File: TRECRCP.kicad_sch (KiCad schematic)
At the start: 46 parts, among them K1 12v Coil Relay, K2 12v Coil Relay, K5 Fujitsu_FTR-LYCA005x, K6 Fujitsu_FTR-LYCA005x, K7 Fujitsu_FTR-LYCA005x, Q2 STF40NF03L, Q3 STF40NF03L, Q4 STF40NF03L, SW1 Dispatch2, SW1 Maint/Off/On Switch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

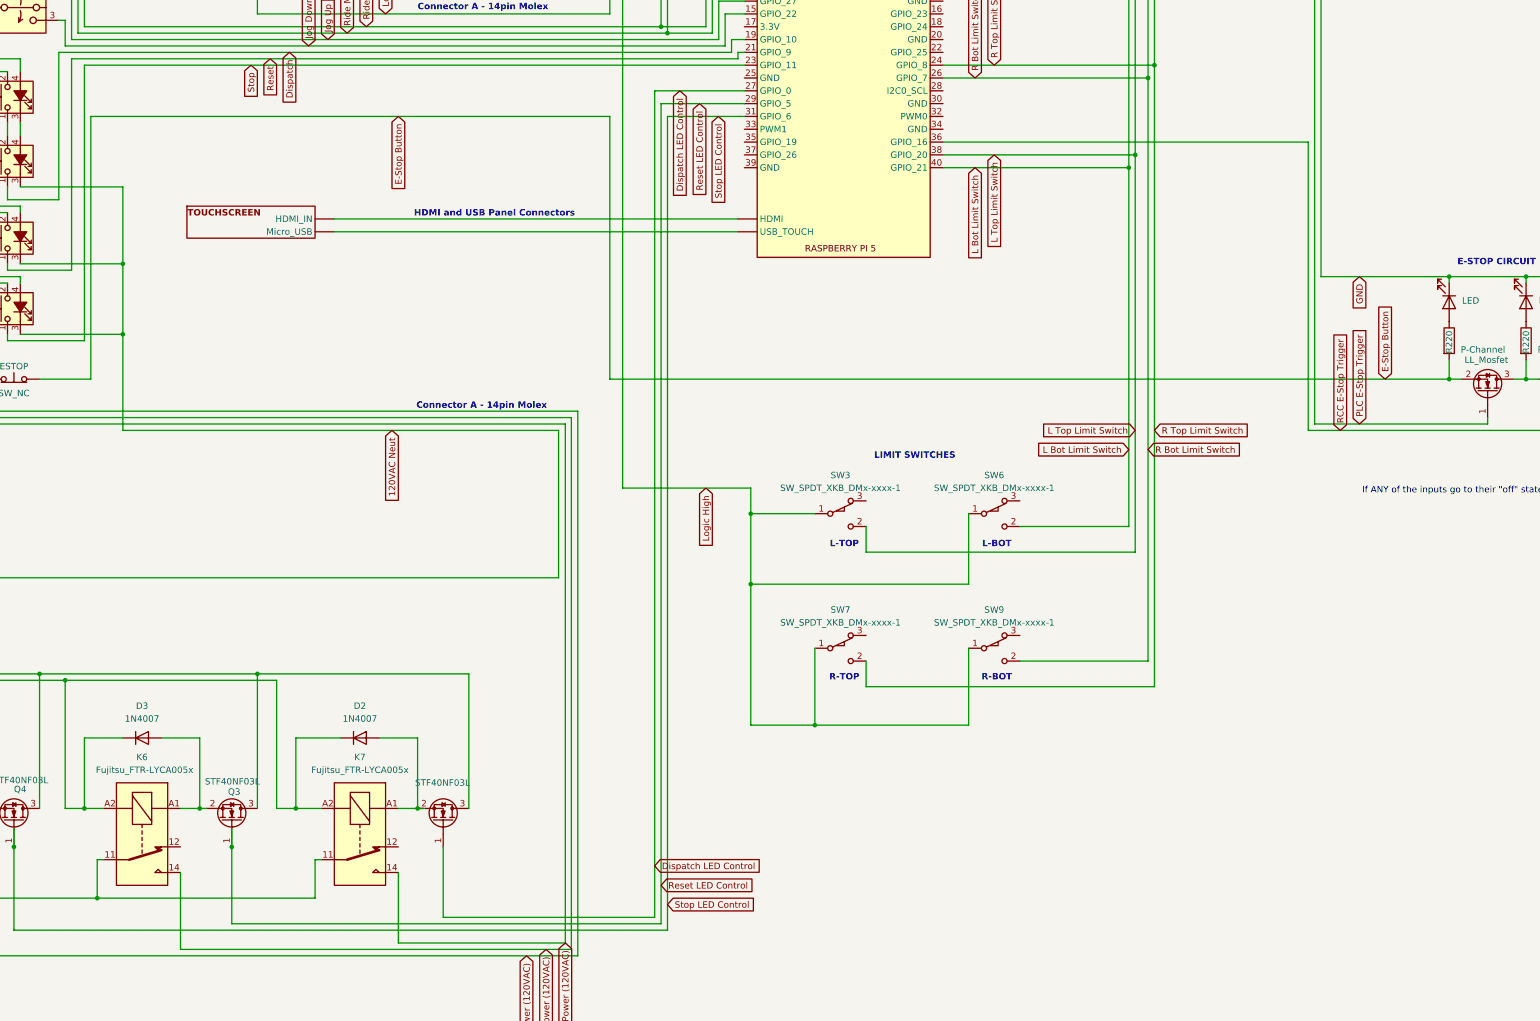
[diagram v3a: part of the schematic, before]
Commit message: update w/ new RCC pin #s
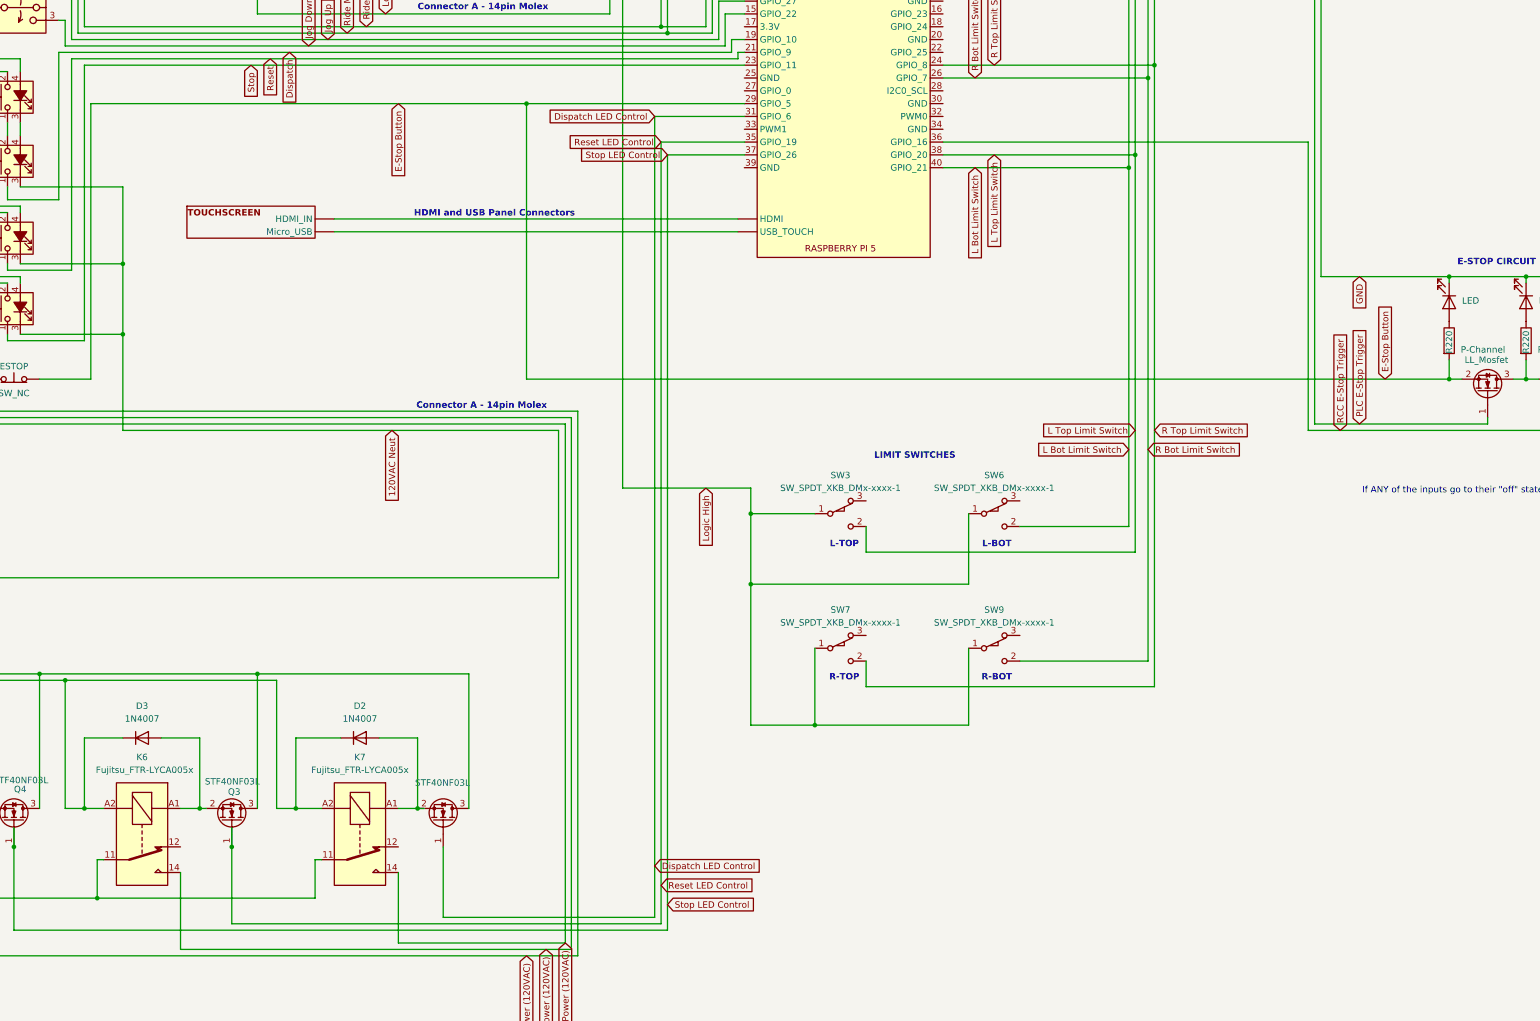
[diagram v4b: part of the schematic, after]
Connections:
- net Dispatch LED Control: now also RCC1.31 (GPIO_6); no longer RCC1.27 (GPIO_0)
- net E-Stop Button: now also RCC1.29 (GPIO_5)
- net Reset LED Control: now also RCC1.35 (GPIO_19); no longer RCC1.29 (GPIO_5)
- net Stop LED Control: now also RCC1.37 (GPIO_26); no longer RCC1.31 (GPIO_6)
- net at RCC1. (USB-C): now also U2.3 (USB-C); no longer U3. (Micro_USB)
- new net: RCC1. (USB-C), U3. (Micro_USB)
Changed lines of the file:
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@@
 	)
 	(junction
+		(at 227.33 168.91)
+		(diameter 0)
+		(color 0 0 0 0)
+	)
+	(junction
 		(at 271.78 250.19)
 		(diameter 0)
@@
 	(wire
 		(pts
-			(xy 252.73 166.37) (xy 252.73 330.2)
+			(xy 252.73 171.45) (xy 252.73 330.2)
 		)
 		(stroke
@@
 	(wire
 		(pts
-			(xy 252.73 166.37) (xy 270.51 166.37)
-		)
-		(stroke
-			(width 0)
-			(type default)
-		)
-	)
-	(wire
-		(pts
 			(xy 204.47 96.52) (xy 298.45 96.52)
 		)
@@
 	(wire
 		(pts
-			(xy 140.97 223.52) (xy 140.97 171.45)
+			(xy 140.97 223.52) (xy 140.97 168.91)
 		)
 		(stroke
@@
 	(wire
 		(pts
+			(xy 255.27 179.07) (xy 270.51 179.07)
+		)
+		(stroke
+			(width 0)
+			(type default)
+		)
+	)
+	(wire
+		(pts
 			(xy 210.82 316.23) (xy 210.82 330.2)
 		)
@@
 	(wire
 		(pts
-			(xy 254 168.91) (xy 254 331.47)
+			(xy 254 176.53) (xy 254 331.47)
 		)
 		(stroke
@@
 	(wire
 		(pts
+			(xy 254 176.53) (xy 270.51 176.53)
+		)
+		(stroke
+			(width 0)
+			(type default)
+		)
+	)
+	(wire
+		(pts
 			(xy 347.98 64.77) (xy 347.98 179.07)
 		)
@@
 	(wire
 		(pts
-			(xy 254 168.91) (xy 270.51 168.91)
-		)
-		(stroke
-			(width 0)
-			(type default)
-		)
-	)
-	(wire
-		(pts
 			(xy 114.3 321.31) (xy 114.3 337.82)
 		)
@@
 	(wire
 		(pts
-			(xy 255.27 171.45) (xy 270.51 171.45)
-		)
-		(stroke
-			(width 0)
-			(type default)
-		)
-	)
-	(wire
-		(pts
 			(xy 127 160.02) (xy 127 162.56)
 		)
@@
 	(wire
 		(pts
+			(xy 227.33 168.91) (xy 270.51 168.91)
+		)
+		(stroke
+			(width 0)
+			(type default)
+			(color 255 0 0 1)
+		)
+	)
+	(wire
+		(pts
 			(xy 185.42 326.39) (xy 142.24 326.39)
 		)
@@
 	(wire
 		(pts
-			(xy 255.27 171.45) (xy 255.27 332.74)
+			(xy 255.27 179.07) (xy 255.27 332.74)
 		)
 		(stroke
@@
 	(wire
 		(pts
+			(xy 252.73 171.45) (xy 270.51 171.45)
+		)
+		(stroke
+			(width 0)
+			(type default)
+		)
+	)
+	(wire
+		(pts
 			(xy 383.54 76.2) (xy 383.54 232.41)
 		)
@@
 	(wire
 		(pts
-			(xy 243.84 171.45) (xy 243.84 223.52)
-		)
-		(stroke
-			(width 0)
-			(type default)
-			(color 255 0 0 1)
-		)
-	)
-	(wire
-		(pts
 			(xy 101.6 160.02) (xy 127 160.02)
 		)
@@
 	(wire
 		(pts
-			(xy 140.97 171.45) (xy 243.84 171.45)
+			(xy 140.97 168.91) (xy 227.33 168.91)
 		)
 		(stroke
@@
 	(wire
 		(pts
-			(xy 243.84 223.52) (xy 410.21 223.52)
+			(xy 227.33 223.52) (xy 410.21 223.52)
 		)
 		(stroke
@@
 	(wire
 		(pts
+			(xy 227.33 168.91) (xy 227.33 223.52)
+		)
+		(stroke
+			(width 0)
+			(type default)
+			(color 255 0 0 1)
+		)
+	)
+	(wire
+		(pts
 			(xy 254 67.31) (xy 254 153.67)
 		)
@@
 	(global_label "Dispatch LED Control"
 		(shape input)
-		(at 257.7235 166.37 270)
+		(at 252.73 171.45 180)
 		(fields_autoplaced yes)
 		(effects
@@
 		)
 		(property "Intersheetrefs" "${INTERSHEET_REFS}"
-			(at 257.7235 189.7958 90)
+			(at 229.3042 171.45 0)
 			(effects
 				(font
@@
 	(global_label "Reset LED Control"
 		(shape input)
-		(at 261.62 168.91 270)
+		(at 254 176.53 180)
 		(fields_autoplaced yes)
 		(effects
@@
 		)
 		(property "Intersheetrefs" "${INTERSHEET_REFS}"
-			(at 261.62 189.3726 90)
+			(at 233.5374 176.53 0)
 			(effects
 				(font
@@
 	(global_label "E-Stop Button"
 		(shape input)
-		(at 201.93 171.45 270)
+		(at 201.93 168.91 270)
 		(fields_autoplaced yes)
 		(effects
@@
 		)
 		(property "Intersheetrefs" "${INTERSHEET_REFS}"
-			(at 201.93 188.5258 90)
+			(at 201.93 185.9858 90)
 			(effects
 				(font
@@
 	(global_label "Stop LED Control"
 		(shape input)
-		(at 265.3624 171.45 270)
+		(at 255.27 179.07 180)
 		(fields_autoplaced yes)
 		(effects
@@
 		)
 		(property "Intersheetrefs" "${INTERSHEET_REFS}"
-			(at 265.3624 190.9448 90)
+			(at 235.7752 179.07 0)
 			(effects
 				(font

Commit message: update mosfets
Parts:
- LL_Mosfet: value STF40NF03L -> IRLZ44NPDB
- Q2, Q3, Q4: value STF40NF03L -> IRLZ44NPBF
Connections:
- net at RCC1. (USB-C): now also U2.3 (USB-C); no longer U3. (Micro_USB)
- new net: RCC1. (USB-C), U3. (Micro_USB)
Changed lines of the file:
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@@
 			)
 		)
-		(property "Value" "STF40NF03L"
-			(at 205.232 303.53 90)
+		(property "Value" "IRLZ44NPBF"
+			(at 206.248 305.308 90)
 			(effects
 				(font
@@
 				)
 				(justify left)
-			)
-		)
-		(property "Value" "STF40NF03L"
-			(at 163.576 303.276 90)
+				(hide yes)
+			)
+		)
+		(property "Value" "IRLZ44NPBF"
+			(at 163.576 305.562 90)
 			(effects
 				(font
@@
 			)
 		)
-		(property "Value" "STF40NF03L"
+		(property "Value" "IRLZ44NPDB"
 			(at 181.102 49.784 90)
 			(effects
@@
 				)
 				(justify left)
-			)
-		)
-		(property "Value" "STF40NF03L"
-			(at 121.666 303.022 90)
-			(effects
-				(font
+				(hide yes)
+			)
+		)
+		(property "Value" "IRLZ44NPBF"
+			(at 119.888 305.308 90)
+			(effects
+				(font

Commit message: change wiring of lim switches for plc
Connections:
- net L Bot Limit Switch: now also SW6.3 (C); no longer SW6.2 (B)
- net L Top Limit Switch: now also SW3.3 (C); no longer SW3.2 (B)
- net R Bot Limit Switch: now also SW9.3 (C); no longer SW9.2 (B)
- net R Top Limit Switch: now also SW7.3 (C); no longer SW7.2 (B)
- net at RCC1. (USB-C): now also U2.3 (USB-C); no longer U3. (Micro_USB)
- new net: RCC1. (USB-C), U3. (Micro_USB)
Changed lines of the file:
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@@
 	(wire
 		(pts
+			(xy 294.64 247.65) (xy 298.45 247.65)
+		)
+		(stroke
+			(width 0)
+			(type default)
+		)
+	)
+	(wire
+		(pts
 			(xy 254 67.31) (xy 341.63 67.31)
 		)
@@
 	(wire
 		(pts
-			(xy 294.64 252.73) (xy 294.64 257.81)
-		)
-		(stroke
-			(width 0)
-			(type default)
-		)
-	)
-	(wire
-		(pts
 			(xy 59.69 119.38) (xy 59.69 281.94)
 		)
@@
 	(wire
 		(pts
+			(xy 299.72 284.48) (xy 351.79 284.48)
+		)
+		(stroke
+			(width 0)
+			(type default)
+		)
+	)
+	(wire
+		(pts
 			(xy 186.69 67.31) (xy 186.69 64.77)
 		)
@@
 	(wire
 		(pts
+			(xy 325.12 247.65) (xy 328.93 247.65)
+		)
+		(stroke
+			(width 0)
+			(type default)
+		)
+	)
+	(wire
+		(pts
 			(xy 22.86 107.95) (xy 29.21 107.95)
 		)
@@
 	(wire
 		(pts
+			(xy 298.45 247.65) (xy 298.45 257.81)
+		)
+		(stroke
+			(width 0)
+			(type default)
+		)
+	)
+	(wire
+		(pts
 			(xy 93.98 308.61) (xy 93.98 293.37)
 		)
@@
 	(wire
 		(pts
+			(xy 298.45 257.81) (xy 347.98 257.81)
+		)
+		(stroke
+			(width 0)
+			(type default)
+		)
+	)
+	(wire
+		(pts
 			(xy 147.32 46.99) (xy 147.32 60.96)
 		)
@@
 	(wire
 		(pts
-			(xy 294.64 284.48) (xy 351.79 284.48)
-		)
-		(stroke
-			(width 0)
-			(type default)
-		)
-	)
-	(wire
-		(pts
 			(xy 124.46 172.72) (xy 124.46 175.26)
 		)
@@
 	(wire
 		(pts
-			(xy 325.12 279.4) (xy 350.52 279.4)
-		)
-		(stroke
-			(width 0)
-			(type default)
-		)
-	)
-	(wire
-		(pts
 			(xy 236.22 231.14) (xy 102.87 231.14)
 		)
@@
 	(wire
 		(pts
+			(xy 330.2 274.32) (xy 330.2 279.4)
+		)
+		(stroke
+			(width 0)
+			(type default)
+		)
+	)
+	(wire
+		(pts
 			(xy 314.96 264.16) (xy 314.96 250.19)
 		)
@@
 	(wire
 		(pts
-			(xy 294.64 279.4) (xy 294.64 284.48)
+			(xy 114.3 223.52) (xy 120.65 223.52)
 		)
 		(stroke
@@
 	(wire
 		(pts
-			(xy 114.3 223.52) (xy 120.65 223.52)
+			(xy 173.99 281.94) (xy 215.9 281.94)
 		)
 		(stroke
@@
 	(wire
 		(pts
-			(xy 173.99 281.94) (xy 215.9 281.94)
+			(xy 328.93 252.73) (xy 346.71 252.73)
 		)
 		(stroke
@@
 	(wire
 		(pts
-			(xy 325.12 252.73) (xy 346.71 252.73)
-		)
-		(stroke
-			(width 0)
-			(type default)
-		)
-	)
-	(wire
-		(pts
 			(xy 22.86 100.33) (xy 71.12 100.33)
 		)
@@
 	(wire
 		(pts
+			(xy 328.93 247.65) (xy 328.93 252.73)
+		)
+		(stroke
+			(width 0)
+			(type default)
+		)
+	)
+	(wire
+		(pts
 			(xy 487.68 95.25) (xy 541.02 95.25)
 		)
@@
 	(wire
 		(pts
+			(xy 294.64 274.32) (xy 299.72 274.32)
+		)
+		(stroke
+			(width 0)
+			(type default)
+		)
+	)
+	(wire
+		(pts
 			(xy 264.16 146.05) (xy 270.51 146.05)
 		)
@@
 	(wire
 		(pts
+			(xy 299.72 274.32) (xy 299.72 284.48)
+		)
+		(stroke
+			(width 0)
+			(type default)
+		)
+	)
+	(wire
+		(pts
 			(xy 271.78 250.19) (xy 284.48 250.19)
 		)
@@
 	(wire
 		(pts
-			(xy 294.64 257.81) (xy 347.98 257.81)
+			(xy 325.12 274.32) (xy 330.2 274.32)
 		)
 		(stroke
@@
 		)
 		(stroke
+			(width 0)
+			(type default)
+		)
+	)
+	(wire
+		(pts
+			(xy 330.2 279.4) (xy 350.52 279.4)
+		)
+		(stroke

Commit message: AS-BUILT CHANGES
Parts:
- added 24V_to_5V: ~, symbol TREC SYMBOL LIB:24v_-{gt}_5v
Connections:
- net +24V: now also 24V_to_5V.1 (24V)
- net E-Stop Button: no longer RCC1.29 (GPIO_5)
- net GND: now also 24V_to_5V.3 (GND)
- net at RCC1. (USB-C): now also U2.3 (USB-C); no longer U3. (Micro_USB)
- new net: RCC1. (USB-C), U3. (Micro_USB)
- new net To Theming 5V: 24V_to_5V.2 (5V)
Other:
- note added: "1"
- note added: "8"
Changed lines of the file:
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@@
 		)
 	)
+	(text "8"
+		(exclude_from_sim no)
+		(at 203.2 162.814 0)
+		(effects
+			(font
+				(size 1.27 1.27)
+			)
+		)
+	)
 	(text "E-STOP CIRCUIT"
 		(exclude_from_sim no)
@@
 		)
 	)
+	(text "1"
+		(exclude_from_sim no)
+		(at 203.2 150.368 0)
+		(effects
+			(font
+				(size 1.27 1.27)
+			)
+		)
+	)
 	(text "LIMIT SWITCHES"
 		(exclude_from_sim no)
@@
 	)
 	(junction
+		(at 447.04 78.74)
+		(diameter 0)
+		(color 0 0 0 0)
+	)
+	(junction
 		(at 410.21 203.2)
 		(diameter 0)
@@
 	)
 	(junction
+		(at 447.04 96.52)
+		(diameter 0)
+		(color 0 0 0 0)
+	)
+	(junction
 		(at 350.52 163.83)
 		(diameter 0)
@@
 	)
 	(junction
+		(at 441.96 95.25)
+		(diameter 0)
+		(color 0 0 0 0)
+	)
+	(junction
 		(at 165.1 60.96)
 		(diameter 0)
@@
 	)
 	(junction
-		(at 227.33 168.91)
-		(diameter 0)
-		(color 0 0 0 0)
-	)
-	(junction
 		(at 271.78 250.19)
 		(diameter 0)
@@
 	(wire
 		(pts
-			(xy 140.97 223.52) (xy 140.97 168.91)
-		)
-		(stroke
-			(width 0)
-			(type default)
-			(color 255 0 0 1)
-		)
-	)
-	(wire
-		(pts
 			(xy 314.96 292.1) (xy 314.96 276.86)
 		)
@@
 	(wire
 		(pts
+			(xy 447.04 78.74) (xy 447.04 96.52)
+		)
+		(stroke
+			(width 0)
+			(type default)
+		)
+	)
+	(wire
+		(pts
 			(xy 284.48 292.1) (xy 314.96 292.1)
 		)
@@
 	(wire
 		(pts
+			(xy 441.96 95.25) (xy 487.68 95.25)
+		)
+		(stroke
+			(width 0)
+			(type default)
+		)
+	)
+	(wire
+		(pts
 			(xy 501.65 182.88) (xy 501.65 212.09)
 		)
@@
 	(wire
 		(pts
+			(xy 447.04 96.52) (xy 485.14 96.52)
+		)
+		(stroke
+			(width 0)
+			(type default)
+		)
+	)
+	(wire
+		(pts
 			(xy 535.94 119.38) (xy 532.13 119.38)
 		)
@@
 	(wire
 		(pts
-			(xy 384.81 96.52) (xy 485.14 96.52)
+			(xy 384.81 96.52) (xy 447.04 96.52)
 		)
 		(stroke
@@
 	(wire
 		(pts
+			(xy 441.96 88.9) (xy 441.96 95.25)
+		)
+		(stroke
+			(width 0)
+			(type default)
+		)
+	)
+	(wire
+		(pts
 			(xy 586.74 160.02) (xy 574.04 160.02)
 		)
@@
 	(wire
 		(pts
-			(xy 295.91 95.25) (xy 487.68 95.25)
+			(xy 295.91 95.25) (xy 441.96 95.25)
 		)
 		(stroke
@@
 	(wire
 		(pts
+			(xy 441.96 64.77) (xy 441.96 68.58)
+		)
+		(stroke
+			(width 0)
+			(type default)
+		)
+	)
+	(wire
+		(pts
 			(xy 173.99 281.94) (xy 215.9 281.94)
 		)
@@
 	(wire
 		(pts
-			(xy 227.33 168.91) (xy 270.51 168.91)
-		)
-		(stroke
-			(width 0)
-			(type default)
-			(color 255 0 0 1)
-		)
-	)
-	(wire
-		(pts
 			(xy 185.42 326.39) (xy 142.24 326.39)
 		)
@@
 	(wire
 		(pts
-			(xy 130.81 223.52) (xy 140.97 223.52)
+			(xy 130.81 223.52) (xy 410.21 223.52)
 		)
 		(stroke
@@
 	(wire
 		(pts
+			(xy 447.04 64.77) (xy 447.04 78.74)
+		)
+		(stroke
+			(width 0)
+			(type default)
+		)
+	)
+	(wire
+		(pts
 			(xy 124.46 214.63) (xy 124.46 215.9)
 		)
@@
 	(wire
 		(pts
-			(xy 140.97 168.91) (xy 227.33 168.91)
-		)
-		(stroke
-			(width 0)
-			(type default)
-			(color 255 0 0 1)
-		)
-	)
-	(wire
-		(pts
 			(xy 134.62 152.4) (xy 135.89 152.4)
 		)
@@
 	(wire
 		(pts
-			(xy 227.33 223.52) (xy 410.21 223.52)
-		)
-		(stroke
-			(width 0)
-			(type default)
-			(color 255 0 0 1)
-		)
-	)
-	(wire
-		(pts
 			(xy 186.69 60.96) (xy 186.69 64.77)
 		)
@@
 	(wire
 		(pts
-			(xy 227.33 168.91) (xy 227.33 223.52)
-		)
-		(stroke
-			(width 0)
-			(type default)
-			(color 255 0 0 1)
-		)
-	)
-	(wire
-		(pts
 			(xy 254 67.31) (xy 254 153.67)
 		)
@@
 		)
 	)
+	(global_label "To Theming 5V"
+		(shape input)
+		(at 441.96 64.77 180)
+		(fields_autoplaced yes)
+		(effects
+			(font
+				(size 1.27 1.27)
+			)
+			(justify right)
+		)
+		(property "Intersheetrefs" "${INTERSHEET_REFS}"
+			(at 424.8236 64.77 0)
+			(effects
+				(font
+					(size 1.27 1.27)
+				)
+				(justify right)
+				(hide yes)
+			)
+		)
+	)
 	(global_label "L Bot Limit Switch"
 		(shape input)
@@
 		)
 	)
+	(global_label "PLC E-Stop Trigger"
+		(shape input)
+		(at 379.73 76.2 90)
+		(fields_autoplaced yes)
+		(effects
+			(font
+				(size 1.27 1.27)
+			)
+			(justify left)
+		)
+		(property "Intersheetrefs" "${INTERSHEET_REFS}"
+			(at 379.73 54.2255 90)
+			(effects
+				(font
+					(size 1.27 1.27)
+				)
+				(justify left)
+				(hide yes)
+			)
+		)
+	)
 	(global_label "Jog Down"
 		(shape input)
@@
 	(global_label "E-Stop Button"
 		(shape input)
-		(at 201.93 168.91 270)
+		(at 200.66 223.52 90)
 		(fields_autoplaced yes)
 		(effects
@@
 				(size 1.27 1.27)
 			)
-			(justify right)
+			(justify left)
 		)
 		(property "Intersheetrefs" "${INTERSHEET_REFS}"
-			(at 201.93 185.9858 90)
+			(at 200.66 206.4442 90)
 			(effects
 				(font
 					(size 1.27 1.27)
 				)
-				(justify right)
+				(justify left)
+				(hide yes)
+			)
+		)
+	)
+	(global_label "RCC E-Stop Trigger"
+		(shape input)
+		(at 332.74 176.53 90)
+		(fields_autoplaced yes)
+		(effects
+			(font
+				(size 1.27 1.27)
+			)
+			(justify left)
+		)
+		(property "Intersheetrefs" "${INTERSHEET_REFS}"
+			(at 332.74 154.3136 90)
+			(effects
+				(font
+					(size 1.27 1.27)
+				)
+				(justify left)
+				(hide yes)
+			)
+		)
+	)
+	(global_label "To Theming GND"
+		(shape input)
+		(at 447.04 64.77 0)
+		(fields_autoplaced yes)
+		(effects
+			(font
+				(size 1.27 1.27)
+			)
+			(justify left)
+		)
+		(property "Intersheetrefs" "${INTERSHEET_REFS}"
+			(at 465.7488 64.77 0)
+			(effects
+				(font
+					(size 1.27 1.27)
+				)
+				(justify left)
 				(hide yes)
 			)
@@
 					(unit 1)
 				)
+			)
+		)
+	)
+	(symbol
+		(lib_name "24v_-{gt}_5v_1")
+		(lib_id "TREC SYMBOL LIB:24v_-{gt}_5v")
+		(at 439.42 81.28 90)
+		(unit 1)
+		(exclude_from_sim no)
+		(in_bom yes)
+		(on_board yes)
+		(dnp no)
+		(fields_autoplaced yes)
+		(property "Reference" "24V_to_5V"
+			(at 435.61 78.7399 90)
+			(effects
+				(font
+					(size 1.27 1.27)
+				)
+				(justify left)
+			)
+		)
+		(property "Value" "~"
+			(at 435.61 80.0099 90)
+			(effects
+				(font
+					(size 1.27 1.27)
+				)
+				(justify left)
+				(hide yes)
+			)
+		)
+		(property "Footprint" ""
+			(at 439.42 81.28 0)
+			(effects
+				(font
+					(size 1.27 1.27)
+				)
+				(hide yes)
+			)
+		)
+		(property "Datasheet" ""
+			(at 439.42 81.28 0)
+			(effects
+				(font
+					(size 1.27 1.27)
+				)
+				(hide yes)
+			)
+		)
+		(property "Description" ""
+			(at 439.42 81.28 0)
+			(effects
+				(font
+					(size 1.27 1.27)
+				)
+				(hide yes)
+			)
+		)
+		(pin "2"
+		)
+		(pin "3"
+		)
+		(pin "1"
+		)
+		(instances
+			(project "TRECRCP"
+				(path "/ea91bab5-2f80-490a-b9b5-c78a73310229"
+					(reference "24V_to_5V")
+					(unit 1)
+				)
